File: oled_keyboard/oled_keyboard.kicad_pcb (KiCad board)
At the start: 2 copper layers, 128.6 x 123.6 mm, 115 parts, among them J1 Conn_01x20_Socket, J10 Conn_01x20_Socket, J11 Conn_01x20_Socket, J12 Conn_01x20_Socket, J2 Conn_01x20_Socket, J3 Conn_01x20_Socket, J4 Conn_01x20_Socket, J5 Conn_01x20_Socket, J6 Conn_01x20_Socket, J7 Conn_01x20_Socket, J8 Conn_01x20_Socket, J9 Conn_01x20_Socket, SW1 SW_Push, SW10 SW_Push, SW11 SW_Push, SW12 SW_Push, SW2 SW_Push, SW3 SW_Push, SW4 SW_Push, SW5 SW_Push, SW6 SW_Push, SW7 SW_Push, SW8 SW_Push, SW9 SW_Push, U1 TPS61088RHLR

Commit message: routing in progress
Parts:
- added NT1: NetTie_2, NetTie:NetTie-2_SMD_Pad0.5mm, F.Cu at (167.8, 96.0)
- moved L1 39.2 mm to (175.8, 83.8), turned to -90 degrees
- moved U1 31.3 mm to (172.8, 92.2), turned to -90 degrees
- moved R8 29.9 mm to (174.8, 88.0)
- moved C11 29.1 mm to (170.5, 83.5)
- moved C12 26.0 mm to (177.8, 90.2)
- moved C10 24.8 mm to (170.5, 85.2)
- moved C13 24.0 mm to (178.2, 95.0)
- moved R6 19.8 mm to (173.8, 97.0), turned to 90 degrees
- moved C9 19.6 mm to (171.0, 88.0)
- moved R7 18.2 mm to (178.2, 96.8), turned to 180 degrees
- moved C16 18.1 mm to (169.2, 98.8), turned to 180 degrees
- moved C8 15.0 mm to (167.8, 90.2), turned to 180 degrees
- moved C15 13.3 mm to (169.2, 101.5), turned to 180 degrees
- moved R4 11.7 mm to (174.5, 100.5), turned to 180 degrees
- moved R5 11.4 mm to (173.8, 103.8), turned to -90 degrees
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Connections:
- A1 pad 10: /CS1 -> /CS4
- A1 pad 11: /CS2 -> /CS5
- A1 pad 12: /CS3 -> /CS6
- A1 pad 13: AGND -> GND
- A1 pad 14: /CS4 -> /CS7
- A1 pad 15: /CS5 -> /CS8
- A1 pad 16: /CS6 -> /CS9
- A1 pad 17: /CS7 -> /CS10
- A1 pad 18: AGND -> GND
- A1 pad 19: /CS8 -> /CS11
- A1 pad 2: /ROW2 -> /COL3
- A1 pad 20: /CS9 -> /CS12
- A1 pad 22: unconnected-(A1-GPIO17-Pad22) -> /ROW4
- A1 pad 23: AGND -> GND
- A1 pad 26: /CS10 -> /ROW3
- A1 pad 27: /CS11 -> /ROW2
- A1 pad 28: AGND -> GND
- A1 pad 29: /CS12 -> unconnected-(A1-GPIO22-Pad29)
- A1 pad 3: AGND -> GND
- A1 pad 31: unconnected-(A1-GPIO26_ADC0-Pad31) -> /DC
- A1 pad 32: unconnected-(A1-GPIO27_ADC1-Pad32) -> /RES
- A1 pad 33: AGND -> GND
- A1 pad 37: AGND -> GND
- A1 pad 38: AGND -> GND
- A1 pad 4: /ROW3 -> /COL2
- A1 pad 5: /ROW4 -> /COL1
- A1 pad 6: /COL1 -> /CS1
- A1 pad 7: /COL2 -> /CS2
- A1 pad 8: AGND -> GND
- A1 pad 9: /COL3 -> /CS3
- C1 pad 2: AGND -> GND
- C10 pad 1: AGND -> GND
- C11 pad 1: AGND -> GND
- C14 pad 2: AGND -> GND
- C15 pad 2: AGND -> GND
- C16 pad 2: AGND -> GND
- C17 pad 2: AGND -> GND
- C18 pad 2: AGND -> GND
- C19 pad 2: AGND -> GND
- C2 pad 2: AGND -> GND
- C20 pad 2: AGND -> GND
- C21 pad 2: AGND -> GND
- C22 pad 2: AGND -> GND
- C23 pad 2: AGND -> GND
- C24 pad 2: AGND -> GND
- C25 pad 2: AGND -> GND
- C26 pad 2: AGND -> GND
- C27 pad 2: AGND -> GND
- C28 pad 2: AGND -> GND
- C29 pad 2: AGND -> GND
- C3 pad 2: AGND -> GND
- C30 pad 2: AGND -> GND
- C31 pad 2: AGND -> GND
- C32 pad 2: AGND -> GND
- C33 pad 2: AGND -> GND
- C34 pad 2: AGND -> GND
- C35 pad 2: AGND -> GND
- C36 pad 2: AGND -> GND
- C37 pad 2: AGND -> GND
- C38 pad 2: AGND -> GND
- C39 pad 2: AGND -> GND
- C4 pad 2: AGND -> GND
- C40 pad 2: AGND -> GND
- C41 pad 2: AGND -> GND
- C42 pad 2: AGND -> GND
- C43 pad 2: AGND -> GND
- C44 pad 2: AGND -> GND
- C45 pad 2: AGND -> GND
- C46 pad 2: AGND -> GND
- C47 pad 2: AGND -> GND
- C48 pad 2: AGND -> GND
- C49 pad 2: AGND -> GND
- C5 pad 2: AGND -> GND
- C50 pad 2: AGND -> GND
- C51 pad 2: AGND -> GND
- C52 pad 2: AGND -> GND
- C53 pad 2: AGND -> GND
- C54 pad 2: AGND -> GND
- C55 pad 2: AGND -> GND
- C56 pad 2: AGND -> GND
- C57 pad 2: AGND -> GND
- C58 pad 2: AGND -> GND
- C59 pad 2: AGND -> GND
- C6 pad 2: AGND -> GND
- J1 pad 10: /SDIN -> /MOSI
- J1 pad 11: /SCLK -> /SCK
- J10 pad 10: /SDIN -> /MOSI
- J10 pad 11: /SCLK -> /SCK
- J11 pad 10: /SDIN -> /MOSI
- J11 pad 11: /SCLK -> /SCK
- J12 pad 10: /SDIN -> /MOSI
- J12 pad 11: /SCLK -> /SCK
- J2 pad 10: /SDIN -> /MOSI
- J2 pad 11: /SCLK -> /SCK
- J3 pad 10: /SDIN -> /MOSI
- J3 pad 11: /SCLK -> /SCK
- J4 pad 10: /SDIN -> /MOSI
- J4 pad 11: /SCLK -> /SCK
- J5 pad 10: /SDIN -> /MOSI
- J5 pad 11: /SCLK -> /SCK
- J6 pad 10: /SDIN -> /MOSI
- J6 pad 11: /SCLK -> /SCK
- J7 pad 10: /SDIN -> /MOSI
- J7 pad 11: /SCLK -> /SCK
- J8 pad 10: /SDIN -> /MOSI
- J8 pad 11: /SCLK -> /SCK
- J9 pad 10: /SDIN -> /MOSI
- J9 pad 11: /SCLK -> /SCK
- L1 pad 1: VUSB -> VBUS
- R1 pad 2: AGND -> GND
- R10 pad 2: AGND -> GND
- R11 pad 2: AGND -> GND
- R12 pad 2: AGND -> GND
- R13 pad 2: AGND -> GND
- R14 pad 2: AGND -> GND
- R15 pad 2: AGND -> GND
- R16 pad 2: AGND -> GND
- R17 pad 2: AGND -> GND
- R2 pad 2: AGND -> GND
- R3 pad 2: AGND -> GND
- R9 pad 2: AGND -> GND
- U1 pad 21: AGND -> GND
- U1 pad 22: AGND -> GND
- U1 pad 23: AGND -> GND
- U1 pad 24: AGND -> GND
- U1 pad 25: AGND -> GND
- U1 pad 26: AGND -> GND
- U1 pad 27: AGND -> GND
- U1 pad 28: AGND -> GND
- U1 pad 29: AGND -> GND
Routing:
- net /SCK: track 0.00 -> 594.0 mm, vias 0 -> 18
- net /MOSI: track 0.00 -> 593.4 mm, vias 0 -> 6
- net /RES: track 0.00 -> 565.6 mm, vias 0 -> 18
- net /DC: track 0.00 -> 554.0 mm, vias 0 -> 18
- net /COL1: track 0.00 -> 178.9 mm, vias 0 -> 1
- net /COL2: track 0.00 -> 158.7 mm, vias 0 -> 1
- net /CS10: track 0.00 -> 147.8 mm, vias 0 -> 2
- net /ROW4: track 0.00 -> 134.4 mm, vias 0 -> 3
- net /COL3: track 0.00 -> 129.7 mm, vias 0 -> 1
- net /CS7: track 0.00 -> 126.5 mm, vias 0 -> 2
- net /CS11: track 0.00 -> 116.0 mm, vias 0 -> 2
- net /ROW3: track 0.00 -> 114.6 mm, vias 0 -> 3
- net /CS4: track 0.00 -> 106.7 mm, vias 0 -> 2
- net /CS8: track 0.00 -> 98.9 mm, vias 0 -> 2
- net /ROW2: track 0.00 -> 97.1 mm, vias 0 -> 3
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
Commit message: routing ok. added gitignore
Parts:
- moved NT1 28.8 mm to (191.6, 112.3), turned to 0 degrees
- moved C13 20.4 mm to (193.4, 108.6)
- moved C12 18.5 mm to (193.4, 100.0)
- moved C29 18.5 mm to (131.7, 88.9)
- moved C45 18.5 mm to (158.7, 88.9)
- moved C46 18.5 mm to (158.7, 117.9)
- moved C53 18.5 mm to (146.9, 88.9)
- moved C58 18.5 mm to (146.9, 117.9)
- moved R6 18.5 mm to (189.4, 106.8)
- moved A1 18.5 mm to (187.3, 56.4)
- moved C52 18.5 mm to (146.9, 61.8)
- moved D2 18.5 mm to (135.3, 37.2)
- moved D3 18.5 mm to (162.3, 37.2)
- moved J8 18.5 mm to (125.7, 141.0)
- moved J9 18.5 mm to (152.7, 54.2)
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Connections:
- C14 pad 1: /VOUT -> VCC
- C15 pad 1: /VOUT -> VCC
- C16 pad 1: /VOUT -> VCC
- C20 pad 1: /VCC -> VCC
- C21 pad 1: /VCC -> VCC
- C28 pad 1: /VCC -> VCC
- C29 pad 1: /VCC -> VCC
- C3 pad 1: /VCC -> VCC
- C30 pad 1: /VCC -> VCC
- C31 pad 1: /VCC -> VCC
- C44 pad 1: /VCC -> VCC
- C45 pad 1: /VCC -> VCC
- C46 pad 1: /VCC -> VCC
- C47 pad 1: /VCC -> VCC
- C5 pad 1: /VCC -> VCC
- C6 pad 1: /VOUT -> VCC
- J1 pad 2: /VCC -> VCC
- J10 pad 2: /VCC -> VCC
- J11 pad 2: /VCC -> VCC
- J12 pad 2: /VCC -> VCC
- J2 pad 2: /VCC -> VCC
- J3 pad 2: /VCC -> VCC
- J4 pad 2: /VCC -> VCC
- J5 pad 2: /VCC -> VCC
- J6 pad 2: /VCC -> VCC
- J7 pad 2: /VCC -> VCC
- J8 pad 2: /VCC -> VCC
- J9 pad 2: /VCC -> VCC
- R5 pad 2: /VOUT -> VCC
- U1 pad 14: /VOUT -> VCC
- U1 pad 15: /VOUT -> VCC
- U1 pad 16: /VOUT -> VCC
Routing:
- net VCC: track 0.00 -> 509.1 mm, vias 0 -> 13
- net VBUS: track 0.00 -> 96.3 mm
- net AGND: track 0.00 -> 37.7 mm, vias 0 -> 2
- net /VCC: track 36.0 -> 0.00 mm
- net /ROW3: track 114.6 -> 130.7 mm
- net /ROW1: track 78.0 -> 93.3 mm
- net /FB: track 0.00 -> 10.3 mm
- net /SW: track 0.00 -> 10.2 mm
- net Net-(U1-COMP): track 0.00 -> 9.51 mm
- net /COL2: track 158.7 -> 153.9 mm
- net /ROW4: track 134.4 -> 130.3 mm
- net Net-(C7-Pad1): track 0.00 -> 3.47 mm
- net Net-(U1-FSW): track 0.00 -> 3.25 mm
- net Net-(U1-BOOT): track 0.00 -> 3.13 mm
- net Net-(U1-ILIM): track 0.00 -> 3.00 mm
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- added copper zone on B.Cu, net GND
- added copper zone on F.Cu, net GND
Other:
- board size 128.6 x 123.6 mm -> 125 x 125 mm

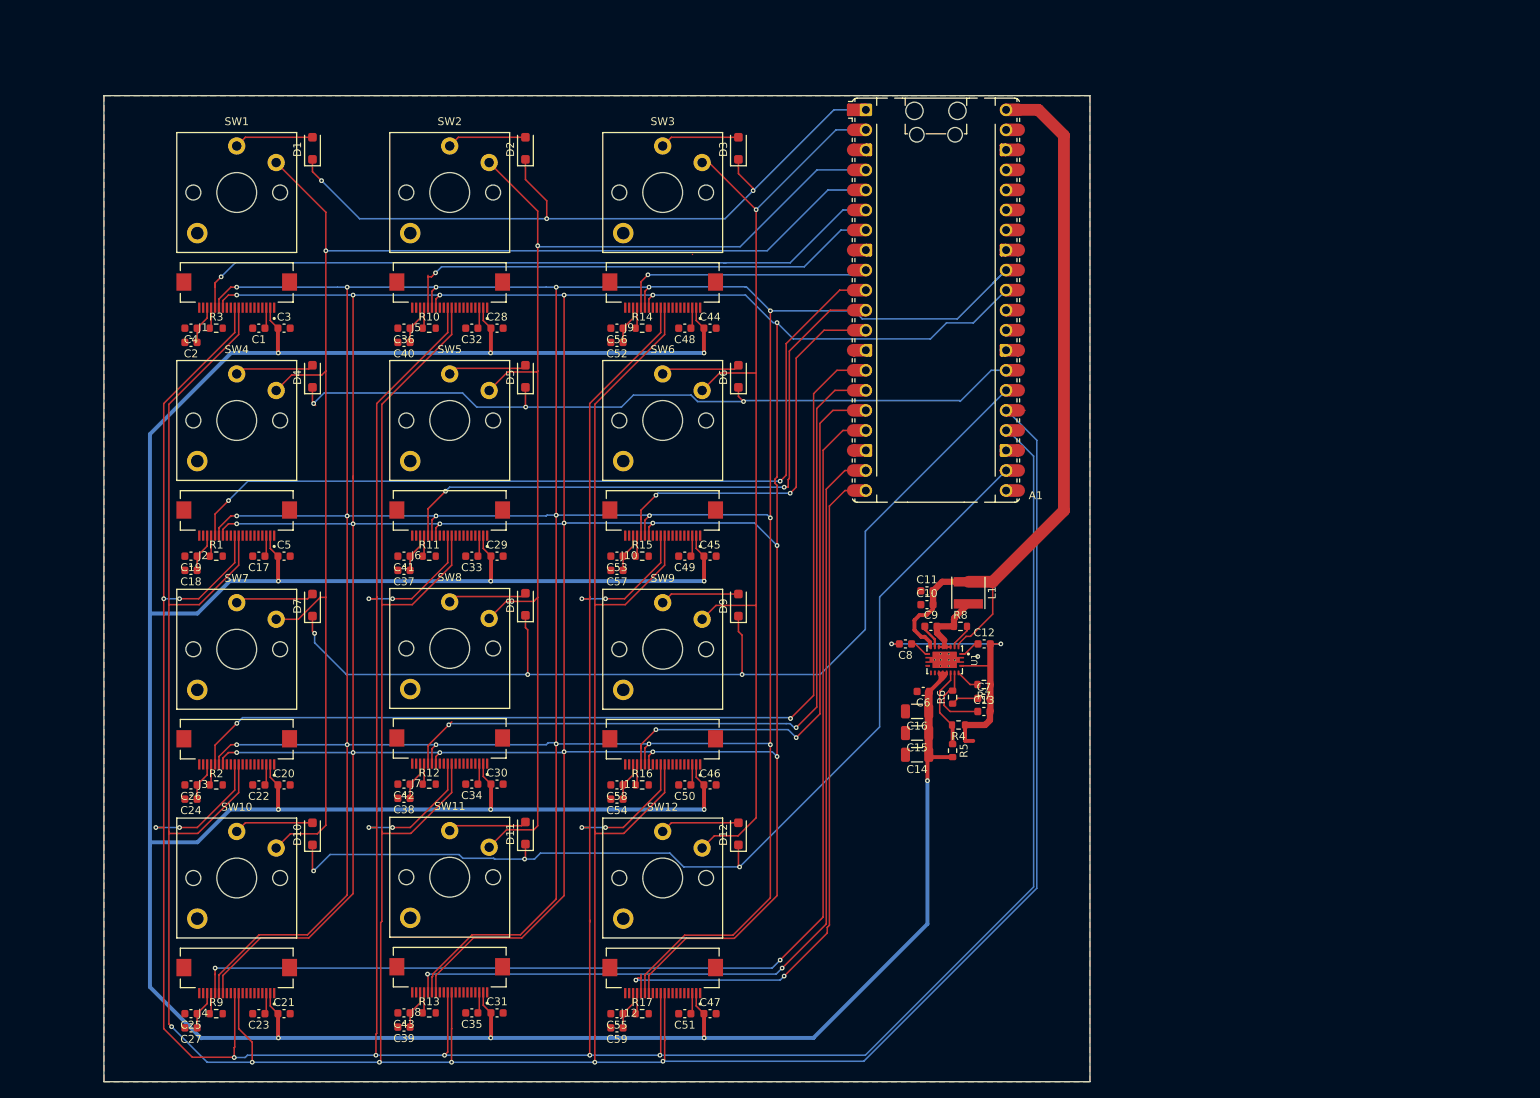
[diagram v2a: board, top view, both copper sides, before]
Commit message: adjusted silkscreen
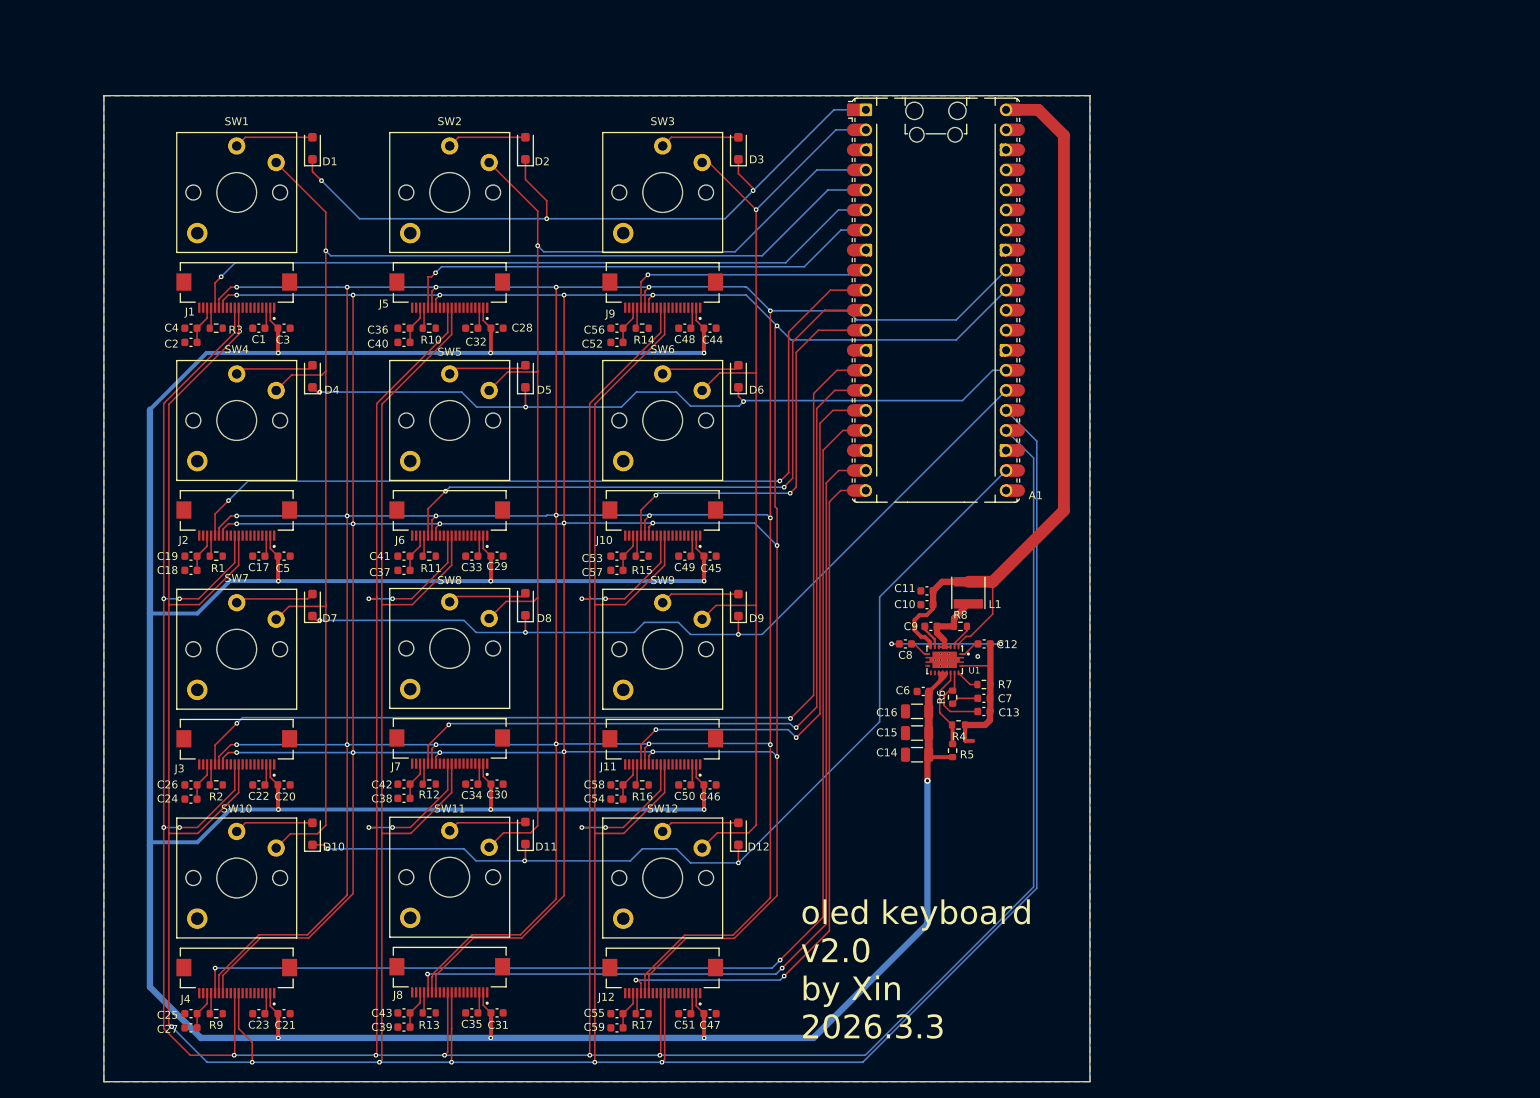
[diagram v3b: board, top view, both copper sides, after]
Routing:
- net /ROW3: track 130.7 -> 107.3 mm
- net /ROW4: track 130.3 -> 124.5 mm
- net /SCK: track 593.4 -> 590.3 mm
- net /RES: track 565.6 -> 562.6 mm
- net /MOSI: track 593.9 -> 591.5 mm
- net /ROW2: track 98.8 -> 96.9 mm
- net VCC: track 509.1 -> 510.9 mm
- net /CS12: track 89.8 -> 88.8 mm
- net /CS4: track 106.0 -> 106.6 mm
- net /COL3: track 128.3 -> 128.8 mm
- net /DC: track 554.0 -> 553.5 mm
- net /CS8: track 98.9 -> 98.3 mm
- net /CS1: track 90.0 -> 89.5 mm
- net /COL2: track 153.9 -> 154.4 mm
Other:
- board text added: "oled keyboard v2.0 by Xin 2026.3.3"

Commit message: added test points
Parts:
- added TP1: TestPoint, TestPoint:TestPoint_Pad_D2.5mm, F.Cu at (184.0, 119.0)
- added TP2: TestPoint, TestPoint:TestPoint_Pad_D2.5mm, F.Cu at (196.0, 90.7)
- added TP3: TestPoint, TestPoint:TestPoint_Pad_D2.5mm, F.Cu at (195.9, 117.3)
- added TP4: TestPoint, TestPoint:TestPoint_Pad_D2.5mm, F.Cu at (195.9, 129.8)
- added TP5: TestPoint, TestPoint:TestPoint_Pad_D2.5mm, F.Cu at (195.9, 123.5)
- added TP6: TestPoint, TestPoint:TestPoint_Pad_D2.5mm, F.Cu at (170.3, 121.3)
- added TP7: TestPoint, TestPoint:TestPoint_Pad_D2.5mm, F.Cu at (170.2, 115.1)
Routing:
- net /MOSI: track 591.5 -> 598.5 mm, vias 6 -> 7
- net /RES: track 562.6 -> 568.3 mm, vias 18 -> 19
- net /SCK: track 590.3 -> 594.2 mm, vias 17 -> 18
- net /DC: track 553.5 -> 556.7 mm
- net VCC: track 510.9 -> 513.8 mm
